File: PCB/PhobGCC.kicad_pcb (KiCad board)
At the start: 2 copper layers, 125.5 x 72.9 mm, 47 parts, among them J1 Conn_01x06_Female, J2 Conn_01x04_Female, J3 Conn_01x01_Male, J4 Conn_01x01_Male, J6 10118194-0001LF, SW1 A, SW10 Dup, SW11 Dright, SW12 Ddown, SW2 B, SW3 X, SW4 Y, SW5 Start, SW6 L, SW7 R, SW8 1825027-5, SW9 Dleft, U1 Teensy3.2, U2 2x DRV5053CAQLPGM Hall Effect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, U3 XC6220B331MR

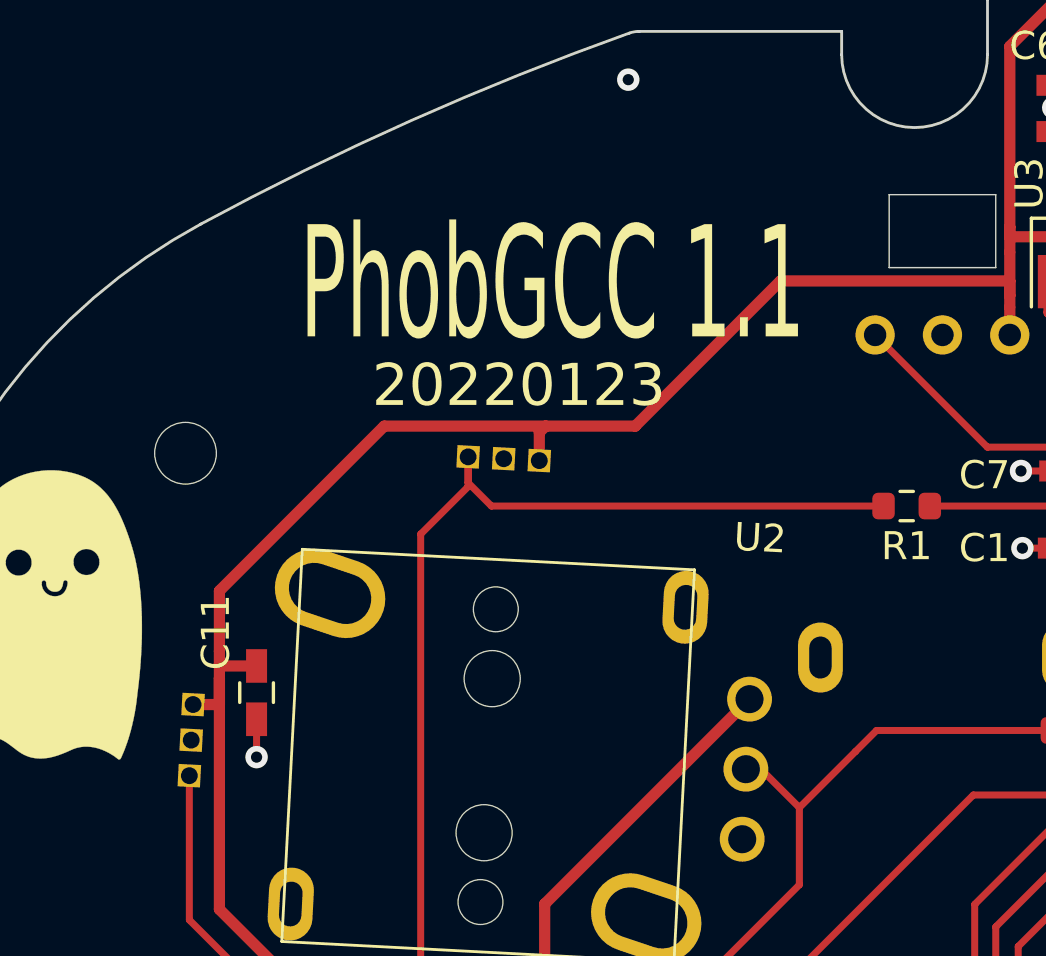
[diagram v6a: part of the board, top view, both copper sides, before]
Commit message: Fixed issue with the linearization fit points, wasn't taking into account how the angles get projected in 3D properly before, giving incorrect values for the 45 degree positions. Started working on alternate hall sensor configuration.
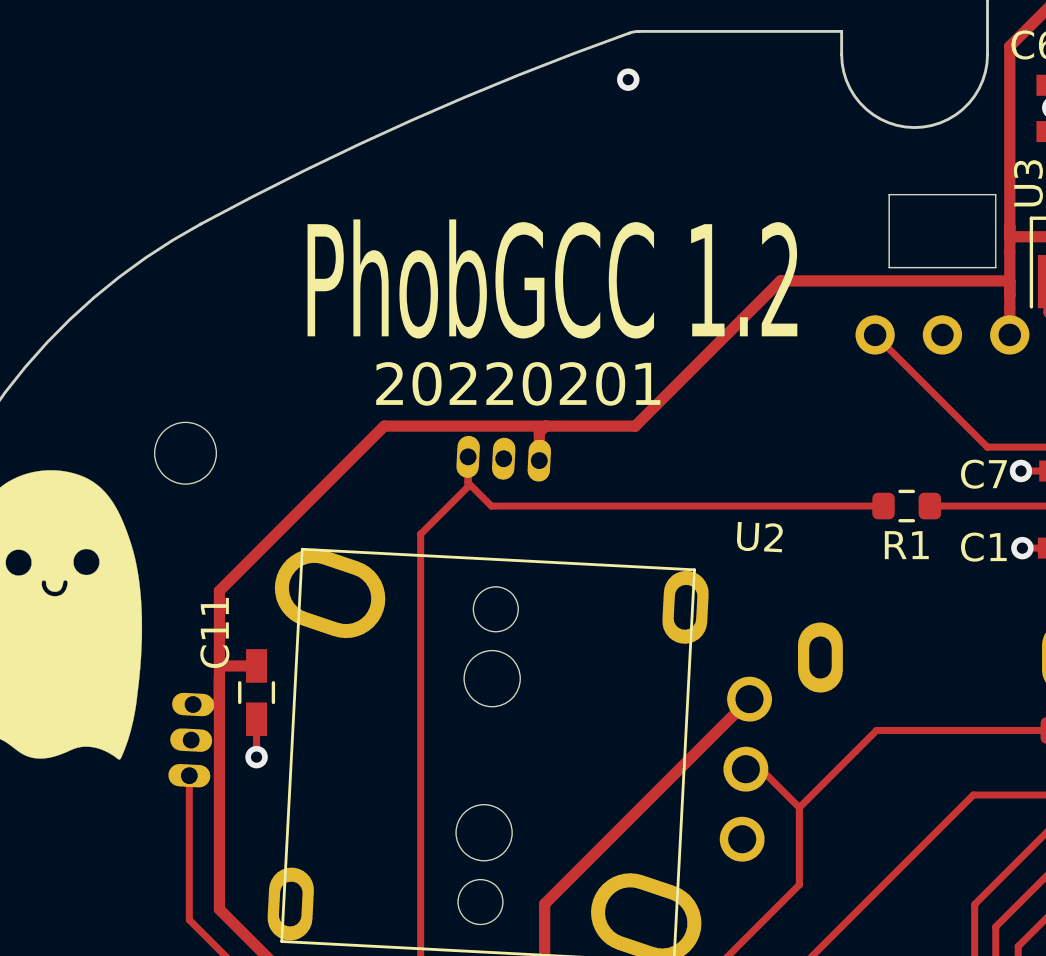
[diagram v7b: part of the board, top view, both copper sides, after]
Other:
- board text added: "20220201"
- board text added: "PhobGCC 1.2"
- board text removed: "20220123"
- board text removed: "PhobGCC 1.1"

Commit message: cleaned manufacturing files for the v1.1 board
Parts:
- C1, C2, C3, C4, C5, C6, C7: value 2200p -> 0.047u
- C10, C11, C12: value 2200p -> 1u
- R1, R2: value 10k -> 2k
- U3: value XC6220B331MR -> ME6206A25XG
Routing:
- net +2V5: track 227.7 -> 228.2 mm
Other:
- board text added: "20220221"
- board text removed: "20220201"
